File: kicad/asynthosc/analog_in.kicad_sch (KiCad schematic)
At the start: 15 parts, among them J2 AudioJack2, J5 AudioJack2, Q1 Q_NPN_BEC, SW1 TRG0, U3 MCP6004

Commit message: sch: wip, add .gitignore
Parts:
- removed unit 2 of U3
- removed unit 3 of U3
- added R11: 47k, Resistor_SMD:R_0603_1608Metric, symbol Device:R
- added R12: 33k, Resistor_SMD:R_0603_1608Metric, symbol Device:R
- added SW2: ${SIM.PARAMS}, symbol Switch:SW_DIP_x01
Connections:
- net GND: now also J2.S, J5.S, R12.2; no longer J2.T, J5.T
- net CVSCAL1: now reaches R1.2
- net CVSCAL1: now also R11.1, R12.1, SW2.2; no longer J2.S
- net at R5.2: now also J5.T; no longer J5.S
- new net: J2.T, R11.2, SW2.1
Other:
- note removed: ".op"
- note removed: ".step param R 1M 0 1M"
- moved on the sheet: C6, D4, D5, J5, R1, R2, R3, R4, U3A

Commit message: sch: wip
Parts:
- removed C6: 1n, Capacitor_SMD:C_0603_1608Metric, symbol Device:C
- removed C7: 100n, Capacitor_SMD:C_0603_1608Metric, symbol Device:C
- removed D4, D5: D_Schottky_1N5817, symbol Device:D_Schottky
- removed J2, J5: AudioJack2, symbol Connector_Audio:AudioJack2
- removed Q1: Q_NPN_BEC, Package_TO_SOT_SMD:SOT-23, symbol Device:Q_NPN_BEC
- removed R1, R2, R5: 100k, Resistor_SMD:R_0603_1608Metric, symbol Device:R
- removed R11: 47k, Resistor_SMD:R_0603_1608Metric, symbol Device:R
- removed R12, R3, R4: 33k, Resistor_SMD:R_0603_1608Metric, symbol Device:R
- removed R6: 10k, Resistor_SMD:R_0603_1608Metric, symbol Device:R
- removed SW1: TRG0, switches:SW_6425, symbol Switch:SW_Push
- removed SW2: ${SIM.PARAMS}, symbol Switch:SW_DIP_x01
- removed unit 4 of U3
- removed unit 1 of U3
- added U3: MCP6004, symbol Amplifier_Operational:MCP6004
- renumbered U3 to U4
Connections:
- net 5V: now also U3.4 (V+)
- net GND: now also U3.11 (V-)
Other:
- added sheet CVin0 (CVin.kicad_sch)
- added sheet CVin1 (CVin.kicad_sch)
- added sheet CVin2 (CVin.kicad_sch)
- added sheet CVin3 (CVin.kicad_sch)
- added sheet Int_in0 (Int_in.kicad_sch)
- note removed: "CV input"
- note removed: "Interrupt input"
- moved on the sheet: U4E

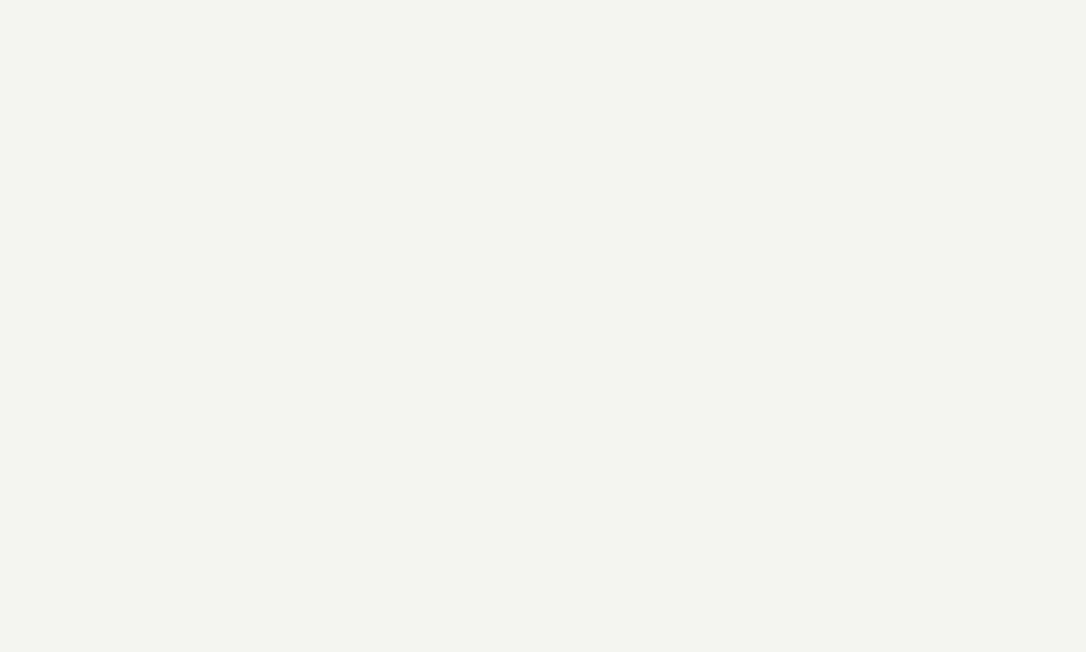
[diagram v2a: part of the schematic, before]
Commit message: sch: update and new interface sheet
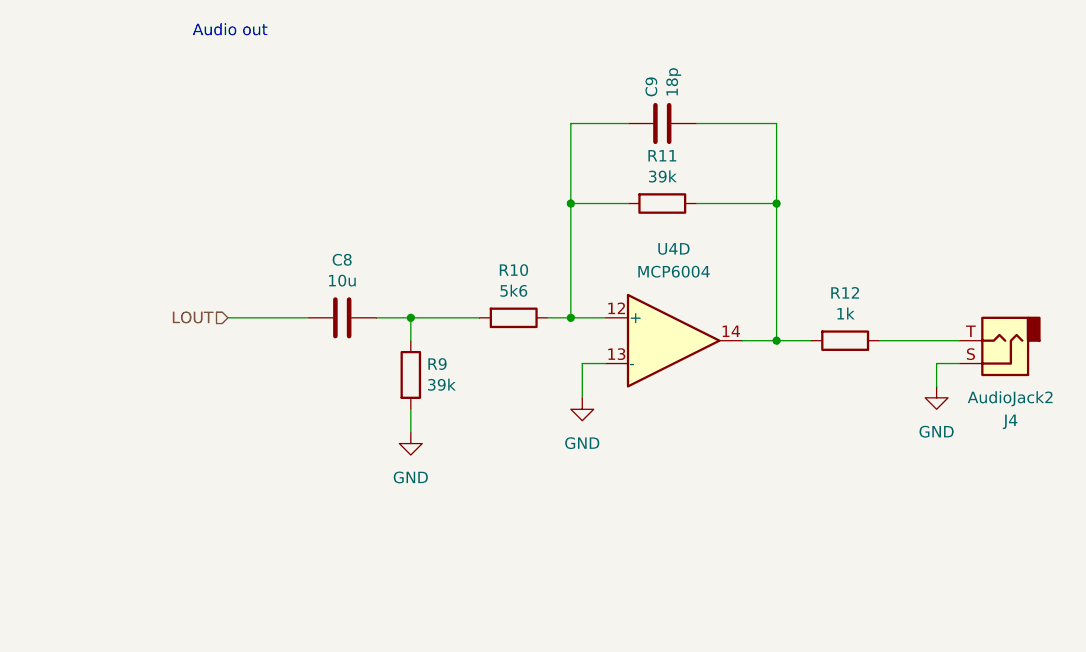
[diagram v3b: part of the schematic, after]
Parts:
- added C8: 10u, Capacitor_SMD:C_0805_2012Metric, symbol Device:C
- added C9: 18p, Capacitor_SMD:C_0603_1608Metric, symbol Device:C
- added J4: AudioJack2, symbol Connector_Audio:AudioJack2
- added R10: 5k6, Resistor_SMD:R_0603_1608Metric, symbol Device:R
- added R11, R9: 39k, Resistor_SMD:R_0603_1608Metric, symbol Device:R
- added R12: 1k, Resistor_SMD:R_0603_1608Metric, symbol Device:R
- added unit 4 of U4
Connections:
- net GND: now also J4.S, R9.2, U4.13 (-)
- new net: C8.1, R10.2, R9.1
- new net: J4.T, R12.1
- new net: C9.1, R10.1, R11.2, U4.12 (+)
- new net: C9.2, R11.1, R12.2, U4.14
- new net LOUT: C8.2
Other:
- note added: "Audio out"

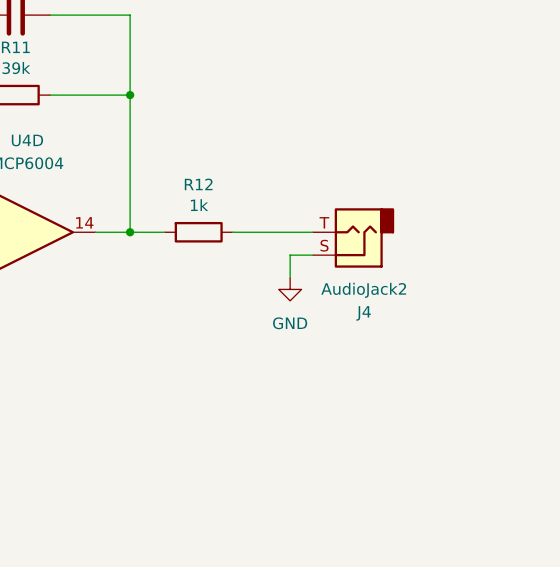
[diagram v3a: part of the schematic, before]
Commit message: sch: add spi nor, display connection, and more footprints
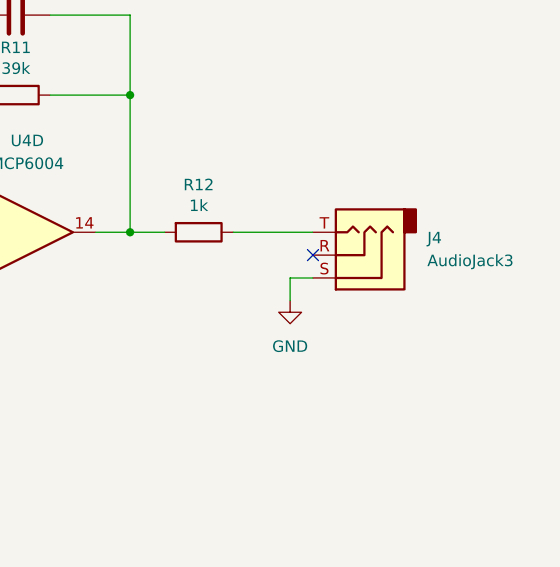
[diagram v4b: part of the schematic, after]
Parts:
- removed J4: AudioJack2, symbol Connector_Audio:AudioJack2
- added J4: AudioJack3, symbol Connector_Audio:AudioJack3
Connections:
- net GND: now also J4.S
- net at R12.1: now also J4.T
- no-connect marks 0 -> 1

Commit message: sch: update footprint links
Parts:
- J4: footprint (none) -> asynthosc:Jack_3.5mm_3legs_XKB_PJ-3411_Vertical
- R10, R11, R12, R9: footprint Resistor_SMD:R_0603_1608Metric -> Resistor_SMD:R_0402_1005Metric
- U3, U4: footprint (none) -> Package_SO:TSSOP-14_4.4x5mm_P0.65mm
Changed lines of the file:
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@@
 			)
 		)
-		(property "Footprint" "Resistor_SMD:R_0603_1608Metric"
+		(property "Footprint" "Resistor_SMD:R_0402_1005Metric"
 			(at 160.782 68.58 90)
 			(effects
@@
 			)
 		)
-		(property "Footprint" ""
+		(property "Footprint" "Package_SO:TSSOP-14_4.4x5mm_P0.65mm"
 			(at 30.48 147.32 0)
 			(effects
@@
 			)
 		)
-		(property "Footprint" "Resistor_SMD:R_0603_1608Metric"
+		(property "Footprint" "Resistor_SMD:R_0402_1005Metric"
 			(at 173.99 60.452 90)
 			(effects
@@
 			)
 		)
-		(property "Footprint" "Resistor_SMD:R_0603_1608Metric"
+		(property "Footprint" "Resistor_SMD:R_0402_1005Metric"
 			(at 190.5 47.752 90)
 			(effects
@@
 			)
 		)
-		(property "Footprint" ""
+		(property "Footprint" "asynthosc:Jack_3.5mm_3legs_XKB_PJ-3411_Vertical"
 			(at 228.6 67.31 0)
 			(effects
@@
 			)
 		)
-		(property "Footprint" "Resistor_SMD:R_0603_1608Metric"
+		(property "Footprint" "Resistor_SMD:R_0402_1005Metric"
 			(at 210.82 62.992 90)
 			(effects
@@
 			)
 		)
-		(property "Footprint" ""
+		(property "Footprint" "Package_SO:TSSOP-14_4.4x5mm_P0.65mm"
 			(at 53.34 147.32 0)
 			(effects
@@
 			)
 		)
-		(property "Footprint" ""
+		(property "Footprint" "Package_SO:TSSOP-14_4.4x5mm_P0.65mm"
 			(at 190.5 62.23 0)
 			(effects

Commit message: wip
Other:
- added sheet Int_in1 (Int_in.kicad_sch)
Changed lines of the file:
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@@
+	(wire
+		(pts
+			(xy 45.72 248.92) (xy 55.88 248.92)
+		)
+		(stroke
+			(width 0)
+			(type default)
+		)
+	)
 	(wire
 		(pts
@@
 		(shape output)
 		(at 55.88 236.22 0)
+		(fields_autoplaced yes)
+		(effects
+			(font
+				(size 1.27 1.27)
+			)
+			(justify left)
+		)
+	)
+	(hierarchical_label "TRG1"
+		(shape output)
+		(at 55.88 248.92 0)
 		(fields_autoplaced yes)
 		(effects
@@
 				)
 			)
+		)
+	)
+	(sheet
+		(at 33.02 245.11)
+		(size 12.7 7.62)
+		(fields_autoplaced yes)
+		(stroke
+			(width 0.1524)
+			(type solid)
+		)
+		(fill
+			(color 0 0 0 0.0000)
+		)
+		(property "Sheetname" "Int_in1"
+			(at 33.02 244.3984 0)
+			(effects
+				(font
+					(size 1.27 1.27)
+				)
+				(justify left bottom)
+			)
+		)
+		(property "Sheetfile" "Int_in.kicad_sch"
+			(at 33.02 253.3146 0)
+			(effects
+				(font
+					(size 1.27 1.27)
+				)
+				(justify left top)
+			)
+		)
+		(pin "TRG" output
+			(at 45.72 248.92 0)
+			(effects
+				(font
+					(size 1.27 1.27)
+				)
+				(justify right)
+			)
+		)
+		(instances
+			(project "asynthosc"
+				(path "/d73e377a-a016-415f-8824-91cc6e4907b9/5f8430bb-1923-4d76-b418-f207310879ec"
+					(page "5")
+				)
+			)

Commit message: sch: change stm32 for smaller one, create smaller jumper footprint
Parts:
- C8, C9: RefNum (none) -> _generic_
- J4: Manufacturer (none) -> XKB; RefNum (none) -> PJ-3411
- U3, U4: Manufacturer (none) -> Microchip; RefNum (none) -> MCP6004
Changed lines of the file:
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@@
+			)
+		)
+		(property "LCSC" ""
+			(at 154.94 62.23 0)
+			(effects
+				(font
+					(size 1.27 1.27)
+				)
+				(hide yes)
+			)
+		)
+		(property "Manufacturer" ""
+			(at 154.94 62.23 0)
+			(effects
+				(font
+					(size 1.27 1.27)
+				)
+				(hide yes)
+			)
+		)
+		(property "RefNum" "_generic_"
+			(at 154.94 62.23 0)
+			(effects
+				(font
+					(size 1.27 1.27)
+				)
+				(hide yes)
 			)
 		)
@@
 			)
 		)
+		(property "LCSC" ""
+			(at 162.56 68.58 0)
+			(effects
+				(font
+					(size 1.27 1.27)
+				)
+				(hide yes)
+			)
+		)
+		(property "Manufacturer" ""
+			(at 162.56 68.58 0)
+			(effects
+				(font
+					(size 1.27 1.27)
+				)
+				(hide yes)
+			)
+		)
 		(pin "1"
 		)
@@
 			)
 		)
+		(property "LCSC" ""
+			(at 31.75 149.86 0)
+			(effects
+				(font
+					(size 1.27 1.27)
+				)
+				(hide yes)
+			)
+		)
+		(property "Manufacturer" "Microchip"
+			(at 31.75 149.86 0)
+			(effects
+				(font
+					(size 1.27 1.27)
+				)
+				(hide yes)
+			)
+		)
+		(property "RefNum" "MCP6004"
+			(at 31.75 149.86 0)
+			(effects
+				(font
+					(size 1.27 1.27)
+				)
+				(hide yes)
+			)
+		)
 		(pin "1"
 		)
@@
 			)
 		)
+		(property "LCSC" ""
+			(at 173.99 62.23 0)
+			(effects
+				(font
+					(size 1.27 1.27)
+				)
+				(hide yes)
+			)
+		)
+		(property "Manufacturer" ""
+			(at 173.99 62.23 0)
+			(effects
+				(font
+					(size 1.27 1.27)
+				)
+				(hide yes)
+			)
+		)
 		(pin "1"
 		)
@@
 			)
 		)
+		(property "LCSC" ""
+			(at 190.5 49.53 0)
+			(effects
+				(font
+					(size 1.27 1.27)
+				)
+				(hide yes)
+			)
+		)
+		(property "Manufacturer" ""
+			(at 190.5 49.53 0)
+			(effects
+				(font
+					(size 1.27 1.27)
+				)
+				(hide yes)
+			)
+		)
 		(pin "1"
 		)
@@
 			)
 		)
+		(property "LCSC" ""
+			(at 228.6 67.31 0)
+			(effects
+				(font
+					(size 1.27 1.27)
+				)
+				(hide yes)
+			)
+		)
+		(property "Manufacturer" "XKB"
+			(at 228.6 67.31 0)
+			(effects
+				(font
+					(size 1.27 1.27)
+				)
+				(hide yes)
+			)
+		)
+		(property "RefNum" "PJ-3411 "
+			(at 228.6 67.31 0)
+			(effects
+				(font
+					(size 1.27 1.27)
+				)
+				(hide yes)
+			)
+		)
 		(pin "S"
 		)
@@
 			)
 		)
+		(property "LCSC" ""
+			(at 210.82 64.77 0)
+			(effects
+				(font
+					(size 1.27 1.27)
+				)
+				(hide yes)
+			)
+		)
+		(property "Manufacturer" ""
+			(at 210.82 64.77 0)
+			(effects
+				(font
+					(size 1.27 1.27)
+				)
+				(hide yes)
+			)
+		)
 		(pin "1"
 		)
@@
 			)
 		)
+		(property "LCSC" ""
+			(at 54.61 149.86 0)
+			(effects
+				(font
+					(size 1.27 1.27)
+				)
+				(hide yes)
+			)
+		)
+		(property "Manufacturer" "Microchip"
+			(at 54.61 149.86 0)
+			(effects
+				(font
+					(size 1.27 1.27)
+				)
+				(hide yes)
+			)
+		)
+		(property "RefNum" "MCP6004"
+			(at 54.61 149.86 0)
+			(effects
+				(font
+					(size 1.27 1.27)
+				)
+				(hide yes)
+			)
+		)
 		(pin "1"
 		)
@@
 			)
 		)
+		(property "LCSC" ""
+			(at 190.5 40.64 0)
+			(effects
+				(font
+					(size 1.27 1.27)
+				)
+				(hide yes)
+			)
+		)
+		(property "Manufacturer" ""
+			(at 190.5 40.64 0)
+			(effects
+				(font
+					(size 1.27 1.27)
+				)
+				(hide yes)
+			)
+		)
+		(property "RefNum" "_generic_"
+			(at 190.5 40.64 0)
+			(effects
+				(font
+					(size 1.27 1.27)
+				)
+				(hide yes)
+			)
+		)
 		(pin "1"
 		)
@@
 			(at 191.77 64.77 0)
 			(effects
+				(font
+					(size 1.27 1.27)
+				)
+				(hide yes)
+			)
+		)
+		(property "LCSC" ""
+			(at 191.77 64.77 0)
+			(effects
+				(font
+					(size 1.27 1.27)
+				)
+				(hide yes)
+			)
+		)
+		(property "Manufacturer" "Microchip"
+			(at 191.77 64.77 0)
+			(effects
+				(font
+					(size 1.27 1.27)
+				)
+				(hide yes)
+			)
+		)
+		(property "RefNum" "MCP6004"
+			(at 191.77 64.77 0)
+			(effects
